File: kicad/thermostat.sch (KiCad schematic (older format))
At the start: 55 parts, among them IC1 LM2596S-5, J1 Display i2c, J31 Conn_02x03_Odd_Even, J6 Screw_Terminal_01x05, T1 SIR424DP, U11 LTC4041, U21 BMP280

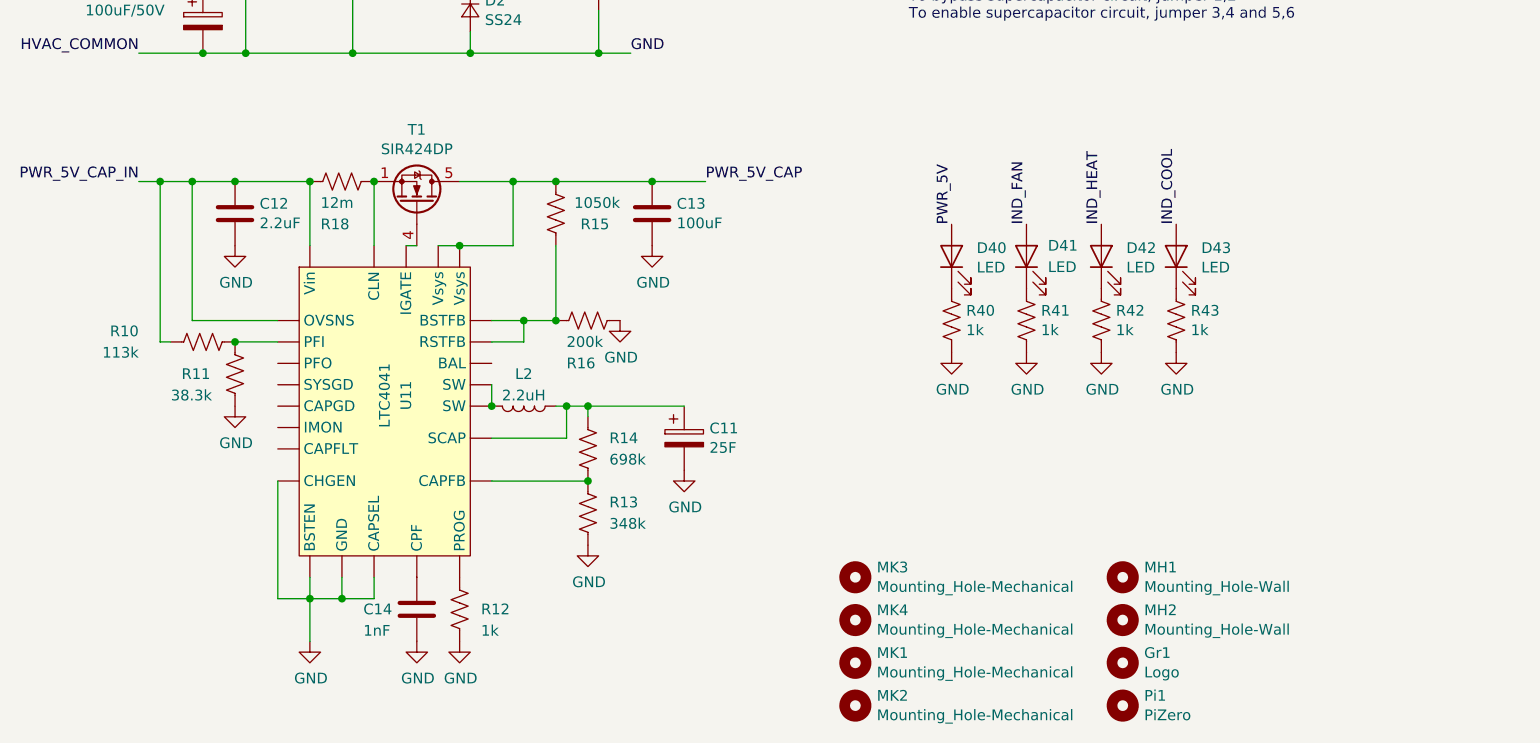
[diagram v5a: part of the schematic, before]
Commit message: Updated ALL references to new library
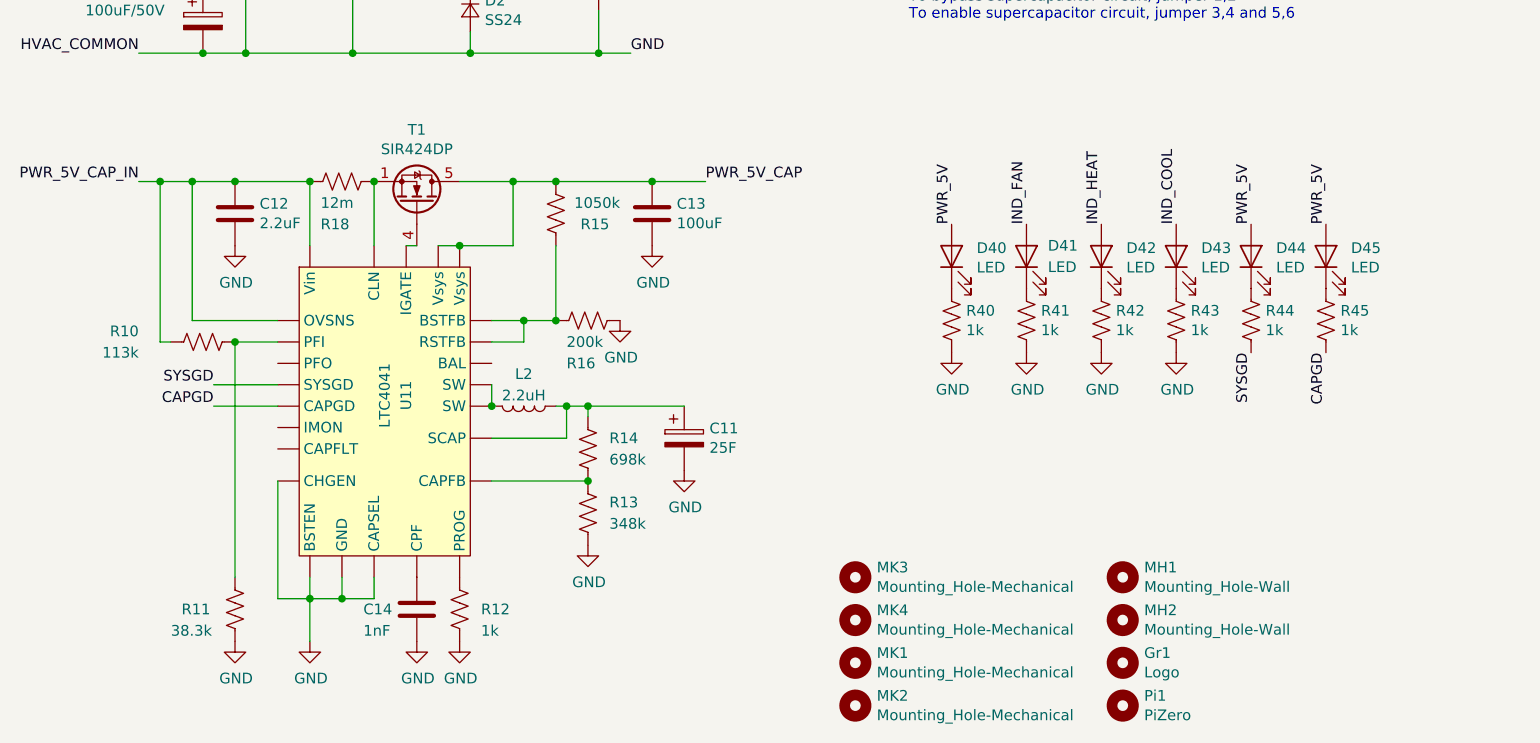
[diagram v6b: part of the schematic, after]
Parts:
- added D44, D45: LED, LED_SMD:LED_0805_2012Metric, symbol Device:LED
- added R44, R45: 1k, Resistor_SMD:R_0805_2012Metric, symbol Device:R_US
- C1, C2: footprint Capacitors_SMD:CP_Elec_8x10 -> Capacitor_SMD:C_Elec_8x10.2
- CONN1: footprint Socket_Strips:Socket_Strip_Straight_2x20_Pitch2.54mm -> Connector_PinSocket_2.54mm:PinSocket_2x20_P2.54mm_Vertical
- D1: footprint Diodes_SMD:D_SOD-123F -> Diode_SMD:D_SOD-123F
- D2: footprint Diodes_SMD:D_SMB -> Diode_SMD:D_SMB
- J1: footprint Pin_Headers:Pin_Header_Straight_1x04_Pitch2.54mm -> Connector_PinSocket_2.54mm:PinSocket_1x04_P2.54mm_Vertical
- J31: footprint Connector_PinHeader_2.54mm:PinHeader_2x03_P2.54mm_Vertical_SMD -> Connector_PinHeader_2.54mm:PinHeader_2x03_P2.54mm_Vertical; Mouser 855-M20-8750342 -> 571-5-146254-3
- L1: footprint Inductors_SMD:L_Wuerth_WE-PD-Typ-M-Typ-S -> Inductor_SMD:L_Wuerth_WE-PD-Typ-M-Typ-S
- MH1, MH2: footprint Mounting_Holes:MountingHole_5mm -> MountingHole:MountingHole_5mm
- MK1, MK2, MK3, MK4: footprint Mounting_Holes:MountingHole_2.5mm_Pad -> MountingHole:MountingHole_2.5mm
- SW_GPIO12, SW_GPIO16, SW_GPIO20, SW_GPIO21: footprint Buttons_Switches_SMD:SW_SPST_EVPBF -> Button_Switch_SMD:SW_SPST_EVPBF
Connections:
- net PWR_5V: now also D44.2 (A), D45.2 (A)
- net SYSGD: now reaches U11.11 (SYSGD)
- net SYSGD: now also R44.2
- net CAPGD: now reaches U11.13 (CAPGD)
- net CAPGD: now also R45.2
- new net: D44.1 (K), R44.1
- new net: D45.1 (K), R45.1
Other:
- moved on the sheet: R11
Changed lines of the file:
@@
 F 0 "CONN1" H 2150 3117 50  0000 C CNN
 F 1 "Conn_02x20_Odd_Even" H 2150 3026 50  0000 C CNN
-F 2 "Socket_Strips:Socket_Strip_Straight_2x20_Pitch2.54mm" H -2750 1050 50  0001 C CNN
-F 3 "https://www.mouser.com/datasheet/2/418/NG_CD_534998_P7-1253073.pdf" H -2750 1050 50  0001 C CNN
+F 2 "Connector_PinSocket_2.54mm:PinSocket_2x20_P2.54mm_Vertical" H -2750 1050 50  0001 C CNN
+F 3 "https://www.mouser.com/datasheet/2/445/61304021821-1626922.pdf" H -2750 1050 50  0001 C CNN
 F 4 "485-2243" H 2100 2000 50  0001 C CNN "Mouser"
 F 5 "1" H 2100 2000 50  0001 C CNN "Populate"
@@
 F 0 "MK1" H 4900 7446 50  0000 L CNN
 F 1 "Mounting_Hole-Mechanical" H 4900 7355 50  0000 L CNN
-F 2 "Mounting_Holes:MountingHole_2.5mm_Pad" H 4800 7400 50  0001 C CNN
+F 2 "MountingHole:MountingHole_2.5mm" H 4800 7400 50  0001 C CNN
 F 3 "" H 4800 7400 50  0001 C CNN
 	1    4800 7400
@@
 F 0 "MK2" H 4900 7646 50  0000 L CNN
 F 1 "Mounting_Hole-Mechanical" H 4900 7555 50  0000 L CNN
-F 2 "Mounting_Holes:MountingHole_2.5mm_Pad" H 4800 7600 50  0001 C CNN
+F 2 "MountingHole:MountingHole_2.5mm" H 4800 7600 50  0001 C CNN
 F 3 "" H 4800 7600 50  0001 C CNN
 	1    4800 7600
@@
 F 0 "MK3" H 4900 7046 50  0000 L CNN
 F 1 "Mounting_Hole-Mechanical" H 4900 6955 50  0000 L CNN
-F 2 "Mounting_Holes:MountingHole_2.5mm_Pad" H 4800 7000 50  0001 C CNN
+F 2 "MountingHole:MountingHole_2.5mm" H 4800 7000 50  0001 C CNN
 F 3 "" H 4800 7000 50  0001 C CNN
 	1    4800 7000
@@
 F 0 "MK4" H 4900 7246 50  0000 L CNN
 F 1 "Mounting_Hole-Mechanical" H 4900 7155 50  0000 L CNN
-F 2 "Mounting_Holes:MountingHole_2.5mm_Pad" H 4800 7200 50  0001 C CNN
+F 2 "MountingHole:MountingHole_2.5mm" H 4800 7200 50  0001 C CNN
 F 3 "" H 4800 7200 50  0001 C CNN
 	1    4800 7200
@@
 F 0 "SW_GPIO16" H 9950 1543 50  0000 C CNN
 F 1 "GPIO16" H 9950 1544 50  0001 C CNN
-F 2 "Buttons_Switches_SMD:SW_SPST_EVPBF" H 9950 1550 50  0001 C CNN
+F 2 "Button_Switch_SMD:SW_SPST_EVPBF" H 9950 1550 50  0001 C CNN
 F 3 "https://www.mouser.com/datasheet/2/315/ATK0000C432-1596775.pdf" H 9950 1550 50  0001 C CNN
 F 4 "667-EVP-BFAC1A000" H 9950 1350 50  0001 C CNN "Mouser"
@@
 F 0 "J1" H 7680 2142 50  0000 L CNN
 F 1 "Display i2c" H 7680 2051 50  0000 L CNN
-F 2 "Pin_Headers:Pin_Header_Straight_1x04_Pitch2.54mm" H 7600 2150 50  0001 C CNN
-F 3 "~" H 7600 2150 50  0001 C CNN
+F 2 "Connector_PinSocket_2.54mm:PinSocket_1x04_P2.54mm_Vertical" H 7600 2150 50  0001 C CNN
+F 3 "https://www.mouser.com/datasheet/2/276/0022284044_PCB_HEADERS-228091.pdf" H 7600 2150 50  0001 C CNN
 F 4 "99" H 7600 2150 50  0001 C CNN "Populate"
 F 5 "538-22-28-4044" H 7600 2150 50  0001 C CNN "Mouser"
@@
 F 0 "D2" V 2954 4418 50  0000 L CNN
 F 1 "SS24" V 3045 4418 50  0000 L CNN
-F 2 "Diodes_SMD:D_SMB" V 3000 4350 50  0001 C CNN
+F 2 "Diode_SMD:D_SMB" V 3000 4350 50  0001 C CNN
 F 3 "https://www.mouser.com/datasheet/2/427/ss22-59686.pdf" V 3000 4350 50  0001 C CNN
 F 4 "625-SS24-E3" V 3000 4350 50  0001 C CNN "Mouser"
@@
 F 0 "L1" H 3300 4065 50  0000 C CNN
 F 1 "150uH" H 3300 3974 50  0000 C CNN
-F 2 "Inductors_SMD:L_Wuerth_WE-PD-Typ-M-Typ-S" H 3300 3850 50  0001 C CNN
+F 2 "Inductor_SMD:L_Wuerth_WE-PD-Typ-M-Typ-S" H 3300 3850 50  0001 C CNN
 F 3 "https://www.mouser.com/datasheet/2/445/7447773151-1526088.pdf" H 3300 3850 50  0001 C CNN
 F 4 "710-7447773151" H 3300 3850 50  0001 C CNN "Mouser"
@@
 F 0 "C2" H 3400 4400 50  0000 L CNN
 F 1 "100uF/50V" H 3100 4300 50  0000 L CNN
-F 2 "Capacitors_SMD:CP_Elec_8x10" H 3638 4050 50  0001 C CNN
+F 2 "Capacitor_SMD:C_Elec_8x10.2" H 3638 4050 50  0001 C CNN
 F 3 "https://www.mouser.com/datasheet/2/315/ABA0000C1184-947404.pdf" H 3600 4200 50  0001 C CNN
 F 4 "667-EEE-FP1H101AV" H 3600 4200 50  0001 C CNN "Mouser"
@@
 F 0 "C1" H 1500 4550 50  0000 L CNN
 F 1 "100uF/50V" H 1200 4450 50  0000 L CNN
-F 2 "Capacitors_SMD:CP_Elec_8x10" H 1788 4250 50  0001 C CNN
+F 2 "Capacitor_SMD:C_Elec_8x10.2" H 1788 4250 50  0001 C CNN
 F 3 "https://www.mouser.com/datasheet/2/315/ABA0000C1184-947404.pdf" H 1750 4400 50  0001 C CNN
 F 4 "667-EEE-FP1H101AV" H 1750 4400 50  0001 C CNN "Mouser"
@@
 F 0 "SW_GPIO20" H 9950 1993 50  0000 C CNN
 F 1 "GPIO20" H 9950 1994 50  0001 C CNN
-F 2 "Buttons_Switches_SMD:SW_SPST_EVPBF" H 9950 2000 50  0001 C CNN
+F 2 "Button_Switch_SMD:SW_SPST_EVPBF" H 9950 2000 50  0001 C CNN
 F 3 "https://www.mouser.com/datasheet/2/315/ATK0000C432-1596775.pdf" H 9950 2000 50  0001 C CNN
 F 4 "667-EVP-BFAC1A000" H 9950 1800 50  0001 C CNN "Mouser"
@@
 F 0 "SW_GPIO21" H 9950 2443 50  0000 C CNN
 F 1 "GPIO21" H 9950 2444 50  0001 C CNN
-F 2 "Buttons_Switches_SMD:SW_SPST_EVPBF" H 9950 2450 50  0001 C CNN
+F 2 "Button_Switch_SMD:SW_SPST_EVPBF" H 9950 2450 50  0001 C CNN
 F 3 "https://www.mouser.com/datasheet/2/315/ATK0000C432-1596775.pdf" H 9950 2450 50  0001 C CNN
 F 4 "667-EVP-BFAC1A000" H 9950 2250 50  0001 C CNN "Mouser"
@@
 F 0 "SW_GPIO12" H 9950 2893 50  0000 C CNN
 F 1 "GPIO12" H 9950 2894 50  0001 C CNN
-F 2 "Buttons_Switches_SMD:SW_SPST_EVPBF" H 9950 2900 50  0001 C CNN
+F 2 "Button_Switch_SMD:SW_SPST_EVPBF" H 9950 2900 50  0001 C CNN
 F 3 "https://www.mouser.com/datasheet/2/315/ATK0000C432-1596775.pdf" H 9950 2900 50  0001 C CNN
 F 4 "667-EVP-BFAC1A000" H 9950 2700 50  0001 C CNN "Mouser"
@@
 F 0 "MH1" H 6150 7046 50  0000 L CNN
 F 1 "Mounting_Hole-Wall" H 6150 6955 50  0000 L CNN
-F 2 "Mounting_Holes:MountingHole_5mm" H 6050 7000 50  0001 C CNN
+F 2 "MountingHole:MountingHole_5mm" H 6050 7000 50  0001 C CNN
 F 3 "" H 6050 7000 50  0001 C CNN
 	1    6050 7000
@@
 F 0 "MH2" H 6150 7246 50  0000 L CNN
 F 1 "Mounting_Hole-Wall" H 6150 7155 50  0000 L CNN
-F 2 "Mounting_Holes:MountingHole_5mm" H 6050 7200 50  0001 C CNN
+F 2 "MountingHole:MountingHole_5mm" H 6050 7200 50  0001 C CNN
 F 3 "" H 6050 7200 50  0001 C CNN
 	1    6050 7200
@@
 L Device:R_US R11
 U 1 1 5E151833
-P 1900 6050
-F 0 "R11" H 1650 6050 50  0000 L CNN
-F 1 "38.3k" H 1600 5950 50  0000 L CNN
-F 2 "Resistor_SMD:R_0805_2012Metric" V 1940 6040 50  0001 C CNN
-F 3 "~" H 1900 6050 50  0001 C CNN
-F 4 "1" H 1900 6050 50  0001 C CNN "Populate"
-	1    1900 6050
+P 1900 7150
+F 0 "R11" H 1650 7150 50  0000 L CNN
+F 1 "38.3k" H 1600 7050 50  0000 L CNN
+F 2 "Resistor_SMD:R_0805_2012Metric" V 1940 7140 50  0001 C CNN
+F 3 "~" H 1900 7150 50  0001 C CNN
+F 4 "1" H 1900 7150 50  0001 C CNN "Populate"
+	1    1900 7150
 	1    0    0    -1
 $EndComp
@@
 L thermostat:GND #PWR0106
 U 1 1 5E21ACCA
-P 1900 6200
-F 0 "#PWR0106" H 1900 5950 50  0001 C CNN
-F 1 "GND" H 1905 6027 50  0000 C CNN
-F 2 "" H 1900 6200 50  0000 C CNN
-F 3 "" H 1900 6200 50  0000 C CNN
-	1    1900 6200
+P 1900 7300
+F 0 "#PWR0106" H 1900 7050 50  0001 C CNN
+F 1 "GND" H 1905 7127 50  0000 C CNN
+F 2 "" H 1900 7300 50  0000 C CNN
+F 3 "" H 1900 7300 50  0000 C CNN
+	1    1900 7300
 	1    0    0    -1
 $EndComp
@@
 Wire Wire Line
 	1900 5900 2100 5900
-Connection ~ 1900 5900
 Wire Wire Line
 	2100 5800 1700 5800
@@
 F 0 "D1" H 1650 3645 50  0000 C CNN
 F 1 "S1A" H 1650 3736 50  0000 C CNN
-F 2 "Diodes_SMD:D_SOD-123F" V 1650 3850 50  0001 C CNN
+F 2 "Diode_SMD:D_SOD-123F" V 1650 3850 50  0001 C CNN
 F 3 "https://www.mouser.com/datasheet/2/308/US1AFA-1301710.pdf" V 1650 3850 50  0001 C CNN
 F 4 "512-US1AFA" H 1650 3850 50  0001 C CNN "Mouser"
@@
 F 0 "J31" H 6000 4367 50  0000 C CNN
 F 1 "Conn_02x03_Odd_Even" H 6000 4276 50  0000 C CNN
-F 2 "Connector_PinHeader_2.54mm:PinHeader_2x03_P2.54mm_Vertical_SMD" H 5950 4050 50  0001 C CNN
-F 3 "https://www.mouser.com/datasheet/2/181/M20-875-1273831.pdf" H 5950 4050 50  0001 C CNN
-F 4 "855-M20-8750342" H 5950 4050 50  0001 C CNN "Mouser"
+F 2 "Connector_PinHeader_2.54mm:PinHeader_2x03_P2.54mm_Vertical" H 5950 4050 50  0001 C CNN
+F 3 "https://www.mouser.com/datasheet/2/418/NG_CD_146254_J2-1238562.pdf" H 5950 4050 50  0001 C CNN
+F 4 "571-5-146254-3" H 5950 4050 50  0001 C CNN "Mouser"
 	1    5950 4050
 	1    0    0    -1
@@
 	1    0    0    -1
 $EndComp
+Wire Wire Line
+	1900 5900 1900 7000
+Connection ~ 1900 5900
+Text Label 1800 6100 2    50   ~ 0
+SYSGD
+Text Label 1800 6200 2    50   ~ 0
+CAPGD
+Wire Wire Line
+	1800 6100 2100 6100
+Wire Wire Line
+	1800 6200 2100 6200
+$Comp
+L Device:LED D44
+U 1 1 5E1242DE
+P 6650 5500
+F 0 "D44" V 6689 5383 50  0000 R CNN
+F 1 "LED" V 6598 5383 50  0000 R CNN
+F 2 "LED_SMD:LED_0805_2012Metric" H 6650 5500 50  0001 C CNN
+F 3 "~" H 6650 5500 50  0001 C CNN
+F 4 "1" H 6650 5500 50  0001 C CNN "Populate"
+	1    6650 5500
+	0    -1   -1   0
+$EndComp
+$Comp
+L Device:R_US R44
+U 1 1 5E1242E5
+P 6650 5800
+F 0 "R44" H 6718 5846 50  0000 L CNN
+F 1 "1k" H 6718 5755 50  0000 L CNN
+F 2 "Resistor_SMD:R_0805_2012Metric" V 6690 5790 50  0001 C CNN
+F 3 "~" H 6650 5800 50  0001 C CNN
+F 4 "1" H 6650 5800 50  0001 C CNN "Populate"
+	1    6650 5800
+	1    0    0    -1
+$EndComp
+Text Label 6650 5350 1    50   ~ 0
+PWR_5V
+Text Label 6650 5950 3    50   ~ 0
+SYSGD
+$Comp
+L Device:LED D45
+U 1 1 5E139FA6
+P 7000 5500
+F 0 "D45" V 7039 5383 50  0000 R CNN
+F 1 "LED" V 6948 5383 50  0000 R CNN
+F 2 "LED_SMD:LED_0805_2012Metric" H 7000 5500 50  0001 C CNN
+F 3 "~" H 7000 5500 50  0001 C CNN
+F 4 "1" H 7000 5500 50  0001 C CNN "Populate"
+	1    7000 5500
+	0    -1   -1   0
+$EndComp
+$Comp
+L Device:R_US R45
+U 1 1 5E139FAD
+P 7000 5800
+F 0 "R45" H 7068 5846 50  0000 L CNN
+F 1 "1k" H 7068 5755 50  0000 L CNN
+F 2 "Resistor_SMD:R_0805_2012Metric" V 7040 5790 50  0001 C CNN
+F 3 "~" H 7000 5800 50  0001 C CNN
+F 4 "1" H 7000 5800 50  0001 C CNN "Populate"
+	1    7000 5800
+	1    0    0    -1
+$EndComp
+Text Label 7000 5350 1    50   ~ 0
+PWR_5V
+Text Label 7000 5950 3    50   ~ 0
+CAPGD
 $EndSCHEMATC

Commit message: small change
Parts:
- T1: footprint Package_SO:PowerPAK_SO-8_Single -> Package_SO:Vishay_PowerPAK_1212-8_Dual; Mouser 781-SIR424DP-GE3 -> 781-SIS434DN-GE3
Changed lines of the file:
@@
 F 0 "T1" V 3092 5250 50  0000 C CNN
 F 1 "SIR424DP" V 3001 5250 50  0000 C CNN
-F 2 "Package_SO:PowerPAK_SO-8_Single" H 2950 5175 50  0001 L CIN
-F 3 "https://www.mouser.com/datasheet/2/427/sir424dp-244427.pdf" V 2750 5250 50  0001 L CNN
-F 4 "781-SIR424DP-GE3" H 2750 5250 50  0001 C CNN "Mouser"
+F 2 "Package_SO:Vishay_PowerPAK_1212-8_Dual" H 2950 5175 50  0001 L CIN
+F 3 "https://www.mouser.com/datasheet/2/427/sis434dn-1324395.pdf" V 2750 5250 50  0001 L CNN
+F 4 "781-SIS434DN-GE3" H 2750 5250 50  0001 C CNN "Mouser"
 	1    2750 5250
 	0    1    -1   0
